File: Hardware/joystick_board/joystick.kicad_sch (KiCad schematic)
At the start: 18 parts, among them J1 Conn_01x40, J2 DE9_Socket_MountingHoles, J3 DE9_Socket_MountingHoles, U1 74HC00, U2 74HC245, U3 74HC245

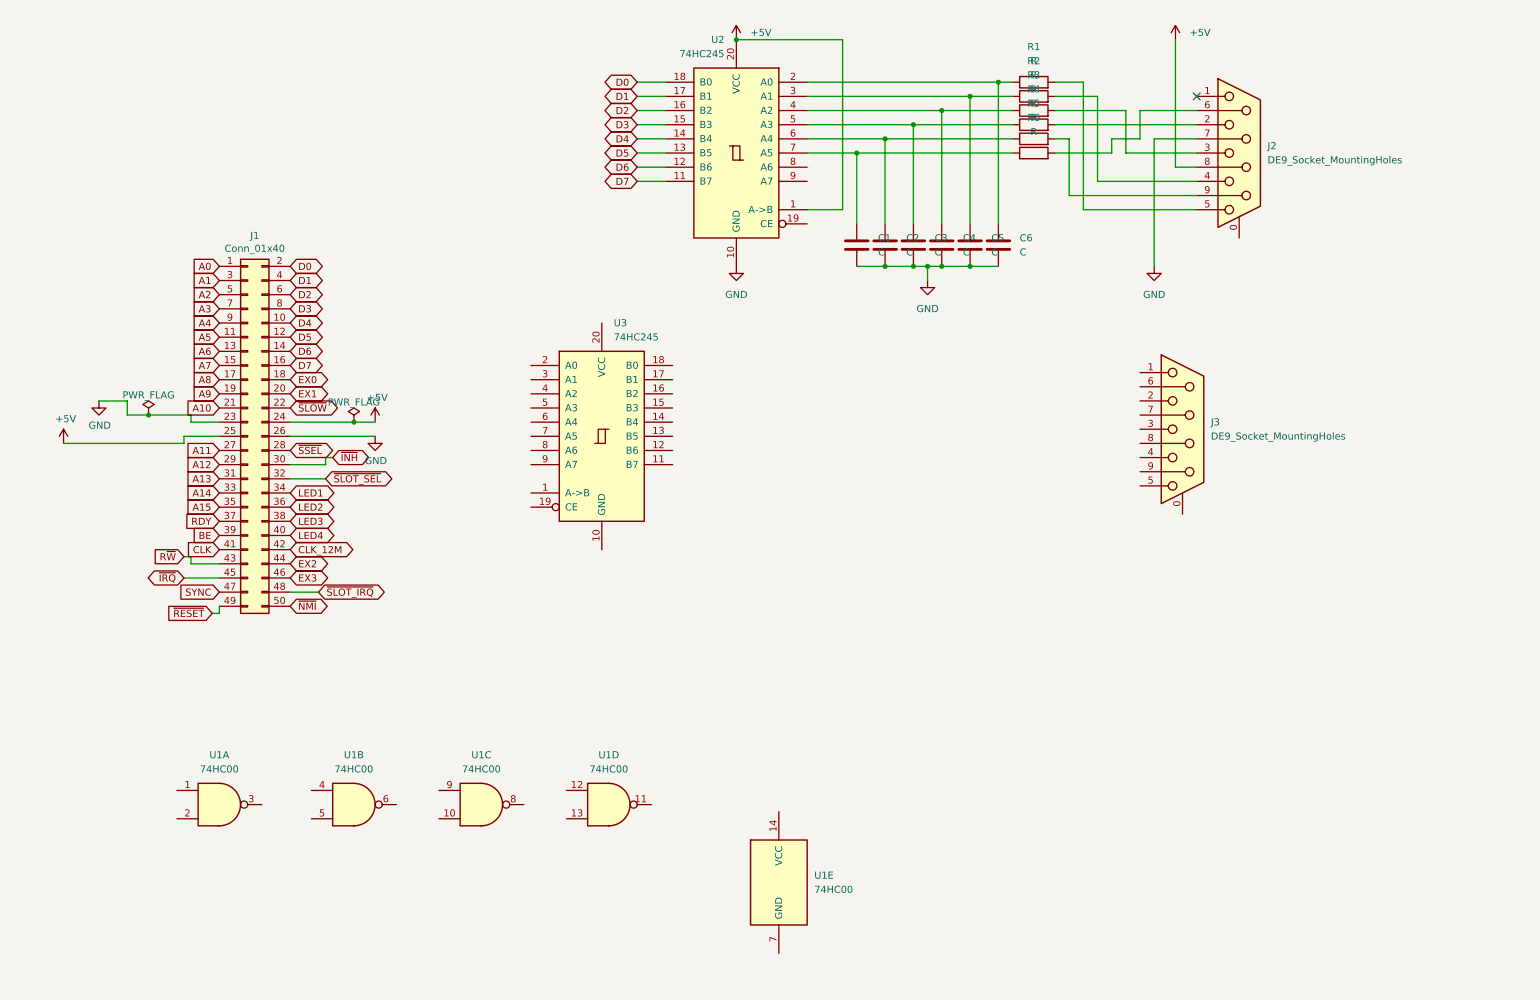
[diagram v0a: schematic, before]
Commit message: some work on joystick pcb, should have all parts now, but joystick port footprints are still to be done
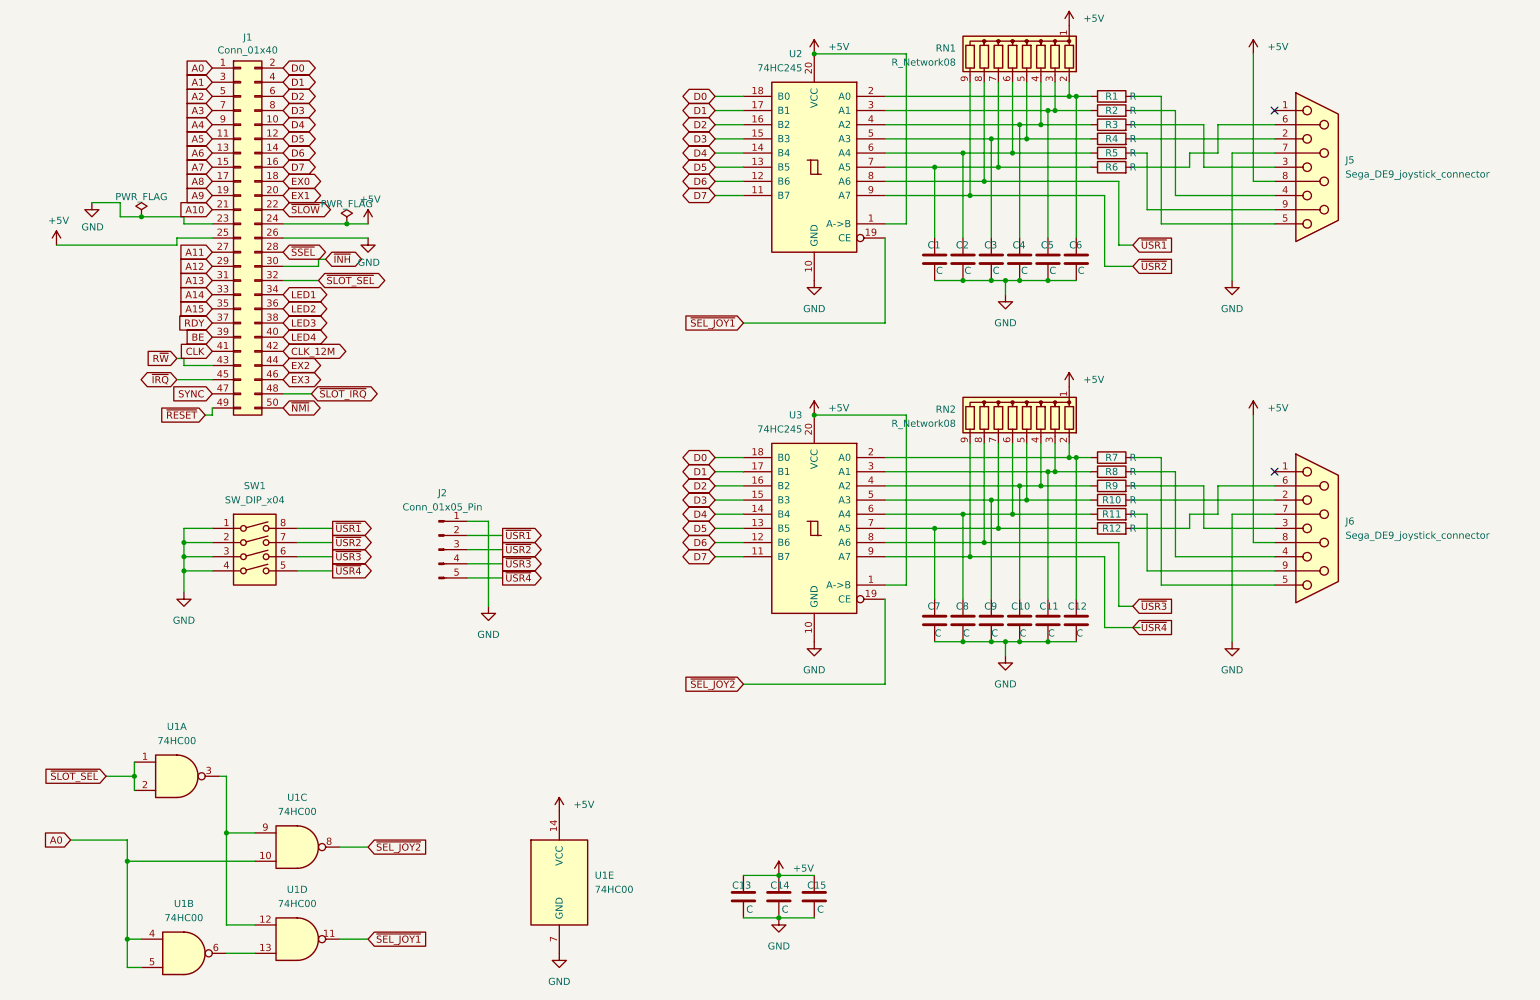
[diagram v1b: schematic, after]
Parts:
- removed J2, J3: DE9_Socket_MountingHoles, Connector_Dsub:DSUB-9_Socket_Horizontal_P2.77x2.84mm_EdgePinOffset4.94mm_Housed_MountingHolesOffset4.94mm, symbol Connector:DE9_Socket_MountingHoles
- added C10, C11, C12, C13, C14, C15, C7, C8, C9: C, Capacitor_THT:C_Disc_D5.0mm_W2.5mm_P2.50mm, symbol Device:C
- added J2: Conn_01x05_Pin, Connector_PinSocket_2.54mm:PinSocket_1x05_P2.54mm_Vertical, symbol Connector:Conn_01x05_Pin
- added J5, J6: Sega_DE9_joystick_connector, Library:Sega DE9 joystick connector, symbol joystick:Sega_DE9_joystick_connector
- added R10, R11, R12, R7, R8, R9: R, Resistor_THT:R_Axial_DIN0204_L3.6mm_D1.6mm_P7.62mm_Horizontal, symbol Device:R
- added RN1, RN2: R_Network08, Resistor_THT:R_Array_SIP9, symbol Device:R_Network08
- added SW1: SW_DIP_x04, Button_Switch_THT:SW_DIP_SPSTx04_Piano_CTS_Series194-4MSTN_W7.62mm_P2.54mm, symbol Switch:SW_DIP_x04
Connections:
- net +5V: now also U1.14 (VCC), U3.1 (A->B), U3.20 (VCC), C13.1, C14.1, C15.1, J5.8, J6.8, RN1.1 (common), RN2.1 (common)
- net A0: now also U1.10, U1.4, U1.5
- net D0: now also U3.18 (B0)
- net D1: now also U3.17 (B1)
- net D2: now also U3.16 (B2)
- net D3: now also U3.15 (B3)
- net D4: now also U3.14 (B4)
- net D5: now also U3.13 (B5)
- net D6: now also U3.12 (B6)
- net D7: now also U3.11 (B7)
- net GND: now also U1.7 (GND), U3.10 (GND), C10.2, C11.2, C12.2, C13.2, C14.2, C15.2, C7.2, C8.2, C9.2, J2.1 (Pin_1), J5.7, J6.7, SW1.1, SW1.2, SW1.3, SW1.4
- net ~{SLOT_SEL}: now also U1.1, U1.2
- net at C5.1, R2.1, U2.3 (A1): now also RN1.3 (R2)
- net at C2.1, R5.1, U2.6 (A4): now also RN1.6 (R5)
- net at R5.2: now also J5.9
- net at R2.2: now also J5.4
- net at U1.3: now also U1.12, U1.9
- net at C4.1, R3.1, U2.4 (A2): now also RN1.4 (R3)
- net at C3.1, R4.1, U2.5 (A3): now also RN1.5 (R4)
- net at R3.2: now also J5.3
- net ~{SEL_JOY2}: now reaches U3.19 (CE)
- net ~{SEL_JOY2}: now also U1.8
- net at U3.2 (A0): now also C12.1, R7.1, RN2.2 (R1)
- net at U3.3 (A1): now also C11.1, R8.1, RN2.3 (R2)
- net at U3.4 (A2): now also C10.1, R9.1, RN2.4 (R3)
- net at U3.5 (A3): now also C9.1, R10.1, RN2.5 (R4)
- net at U3.6 (A4): now also C8.1, R11.1, RN2.6 (R5)
- net at U3.7 (A5): now also C7.1, R12.1, RN2.7 (R6)
- net ~{USR3}: now reaches U3.8 (A6)
- net ~{USR3}: now also J2.4 (Pin_4), RN2.8 (R7), SW1.6
- net ~{USR4}: now reaches U3.9 (A7)
- net ~{USR4}: now also J2.5 (Pin_5), RN2.9 (R8), SW1.5
- net at C1.1, R6.1, U2.7 (A5): now also RN1.7 (R6)
- net ~{SEL_JOY1}: now reaches U2.19 (CE)
- net ~{SEL_JOY1}: now also U1.11
- net at C6.1, R1.1, U2.2 (A0): now also RN1.2 (R1)
- net ~{USR1}: now reaches U2.8 (A6)
- net ~{USR1}: now also J2.2 (Pin_2), RN1.8 (R7), SW1.8
- net ~{USR2}: now reaches U2.9 (A7)
- net ~{USR2}: now also J2.3 (Pin_3), RN1.9 (R8), SW1.7
- net at R6.2: now also J5.6
- net at R4.2: now also J5.2
- net at R1.2: now also J5.5
- net at U1.6: now also U1.13
- new net: J6.6, R12.2
- new net: J6.2, R10.2
- new net: J6.3, R9.2
- new net: J6.4, R8.2
- new net: J6.5, R7.2
- new net: J6.9, R11.2
- no-connect marks 1 -> 2
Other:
- moved on the sheet: C1, C2, C3, C4, C5, C6, J1, R1, R2, R3, R4, R5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
